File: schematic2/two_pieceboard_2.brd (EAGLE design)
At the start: 46 x 40.1 mm, 21 parts, among them J1 2X5P-2.54, Q1 MOSFET-NCHANNELFDD8580, Q2 MOSFET-NCHANNELFDD8580, Q4 MOSFET-NCHANNELFDD8580, Q5 MOSFET-NCHANNELFDD8580, Q6 MOSFET-NCHANNELFDD8580, Q7 MOSFET-NCHANNELFDD8580, U3 LM317DCY

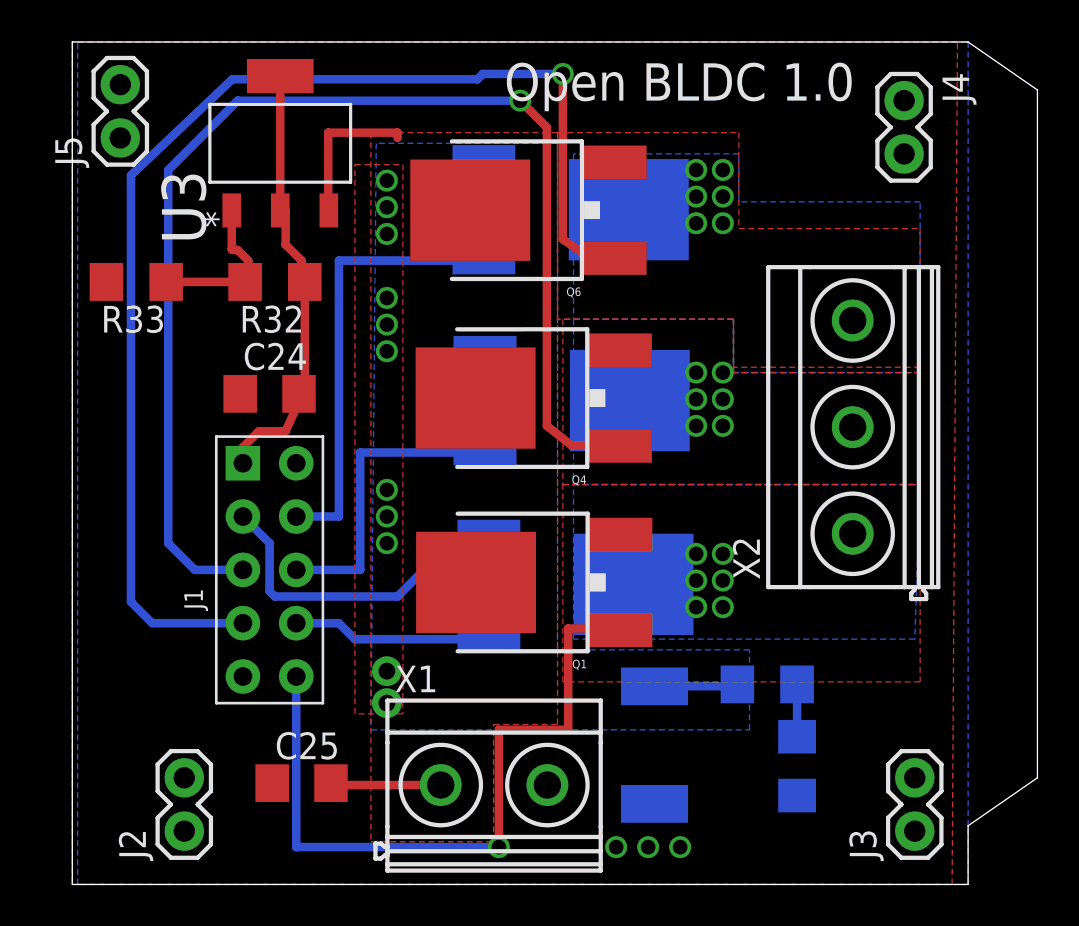
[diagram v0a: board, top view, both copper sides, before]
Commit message: added lower line for upper transistor for all three half bridges to connector.
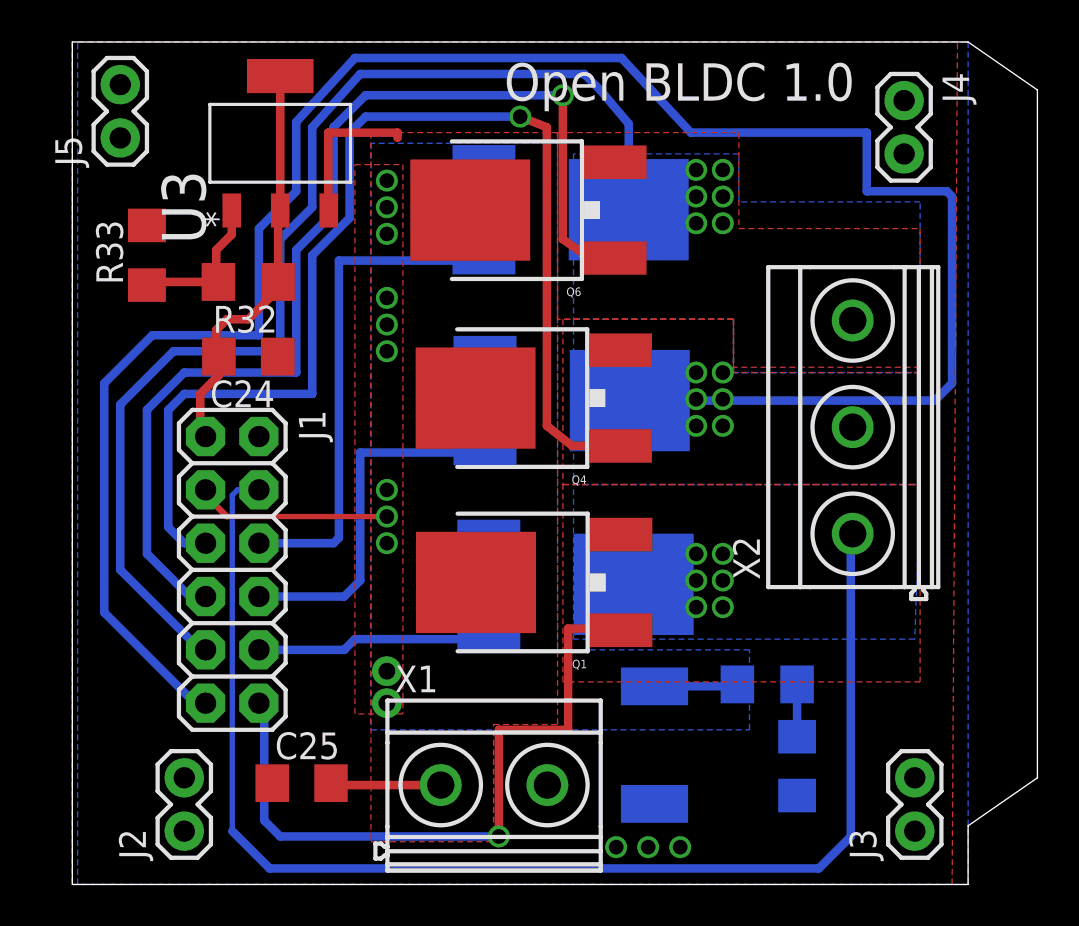
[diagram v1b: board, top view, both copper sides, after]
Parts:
- J1: value 2X5P-2.54 -> 2X6 FEMALE; device Seeed-OPL-Connector:H2X5-2.54 -> SparkFun-Connectors:2X6
- moved J1 7.04 mm to (69.6, 48.0), turned to 270 degrees
- moved C24 2.05 mm to (71.6, 51.8), turned to 180 degrees
- moved R33 1.37 mm to (66.8, 56.6), turned to 90 degrees
- moved R32 1.27 mm to (71.6, 55.4)
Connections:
- net BLDC1: now also J1.4
- net BLDC2: now also J1.11
- net BLDC3: now also J1.9
- net CURRENT: now also J1.3; no longer J1.2
- net GND: now also J1.2; no longer J1.10
- net N$1: now also J1.12; no longer J1.6
- net N$16: now also J1.5; no longer J1.3
- net N$2: now also J1.10; no longer J1.7
- net N$7: now also J1.7; no longer J1.4
- net N$8: now also J1.6; no longer J1.9
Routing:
- net BLDC2: track 0.00 -> 98.4 mm
- net BLDC1: track 0.00 -> 62.7 mm
- net BLDC3: track 0.00 -> 54.9 mm
- net N$7: track 59.2 -> 51.9 mm
- net CURRENT: track 18.9 -> 13.3 mm
- net N$16: track 59.8 -> 55.9 mm
- net N$8: track 21.3 -> 24.2 mm
- net N$6: track 14.7 -> 17.3 mm
- net N$2: track 9.63 -> 11.3 mm
- net +12V: track 20.9 -> 19.6 mm
- net N$1: track 34.5 -> 33.4 mm
